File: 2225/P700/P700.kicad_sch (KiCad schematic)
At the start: 2 parts

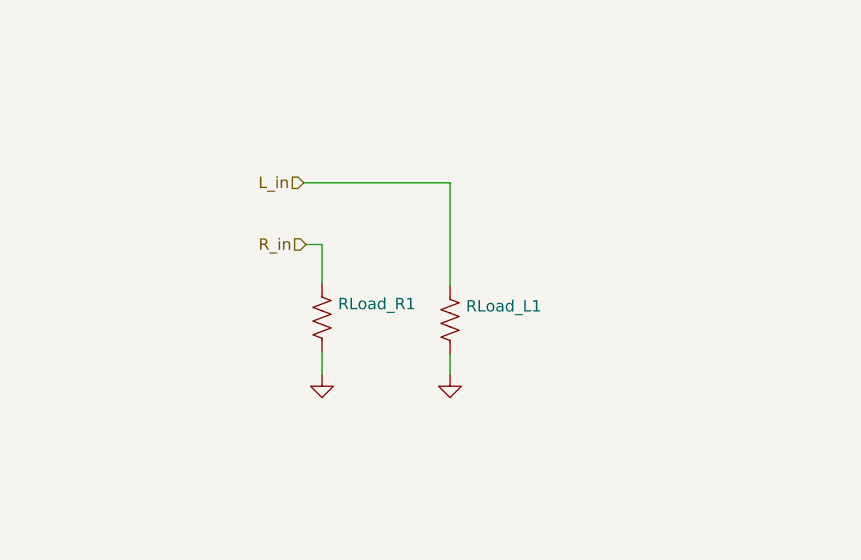
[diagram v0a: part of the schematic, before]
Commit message: Added dummy power inputs to P700 block in 2225.kicad_sch (system block diagram)
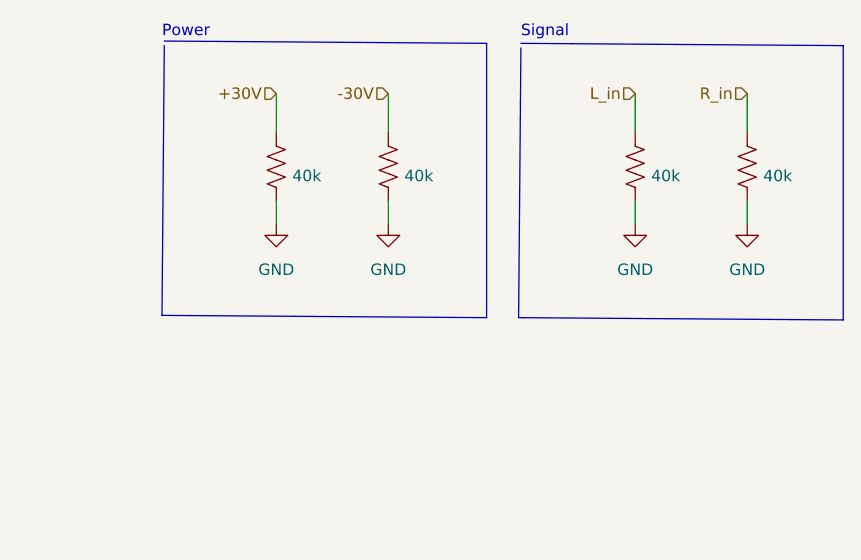
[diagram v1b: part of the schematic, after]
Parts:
- removed RLoad_L1, RLoad_R1: (no value), symbol Device:R_US
- added RLoad_P700_pos1, RLoad_P700_pos? (x3): 40k, Resistor_THT:R_Axial_DIN0309_L9.0mm_D3.2mm_P12.70mm_Horizontal, symbol Device:R_US
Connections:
- net GND: now also RLoad_P700_pos1.1, RLoad_P700_pos?.1, RLoad_P700_pos?.1, RLoad_P700_pos?.1
- net L_in: now also RLoad_P700_pos?.2
- net R_in: now also RLoad_P700_pos?.2
- new net +30V: RLoad_P700_pos1.2
- new net -30V: RLoad_P700_pos?.2
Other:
- note added: "Power"
- note added: "Signal"

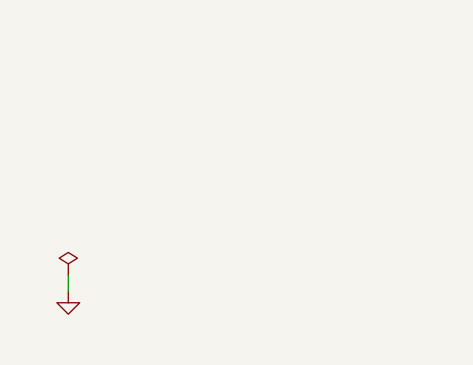
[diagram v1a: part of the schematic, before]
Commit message: Initial system block diagram of 2225
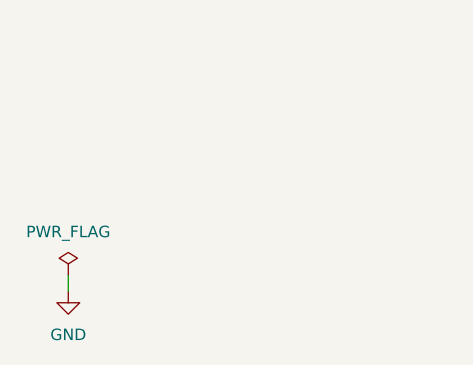
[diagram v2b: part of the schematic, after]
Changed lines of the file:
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@@
       (effects (font (size 1.27 1.27)) hide)
     )
-    (property "Value" "" (id 1) (at 23.876 177.292 0))
+    (property "Value" "PWR_FLAG" (id 1) (at 23.876 177.292 0))
     (property "Footprint" "" (id 2) (at 23.876 182.118 0)
       (effects (font (size 1.27 1.27)) hide)
@@
       (effects (font (size 1.27 1.27)) hide)
     )
-    (property "Value" "" (id 1) (at 23.876 188.722 0))
+    (property "Value" "GND" (id 1) (at 23.876 188.722 0))
     (property "Footprint" "" (id 2) (at 23.876 183.896 0)
       (effects (font (size 1.27 1.27)) hide)
